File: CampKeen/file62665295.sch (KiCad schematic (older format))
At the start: 23 parts

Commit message: updated the pin mapping to the terms. cleaned up the Schematic. PCB placement and routing is what is left to do.
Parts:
- C16, C17, C18, C19: renamed from C?; footprint (none) -> Capacitor_THT:C_Disc_D4.7mm_W2.5mm_P5.00mm
- Q4: renamed from Q?; footprint TO254P469X1042X1967-3P -> SamacSys_Parts:TO254P469X1042X1967-3P
- Z1: renamed from Z?; footprint DIOAD1068W53L380D172 -> SamacSys_Parts:DIOAD1068W53L380D172
- gave numbers to parts that had none: 17

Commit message: separated the 12 and 5 volt outputs. added another spare output.
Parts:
- renumbered Q3 to Q2, Q4 to Q3, Q5 to Q4, Q6 to Q5, Q7 to Q6, Q8 to Q7, R12 to R15, R13 to R16, R14 to R17, R15 to R18, R16 to R19, R17 to R20, R18 to R21, R19 to R22, R20 to R23, R21 to R24, R22 to R25

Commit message: some annotation.
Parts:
- removed Tanks1: TanksVS, SamacSys_Parts:BK_HTC-15M, symbol SamacSys_Parts:BK_HTC-15M
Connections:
- net +BATT: now also Q3.3, R16.1, Z1.1
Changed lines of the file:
@@
 $Descr A4 11693 8268
 encoding utf-8
-Sheet 2 10
+Sheet 5 10
 Title ""
 Date ""
@@
 Connection ~ 6350 3200
 $Comp
-L SamacSys_Parts:BK_HTC-15M Tanks1
-U 1 1 626F6AAA
-P 4200 1800
-AR Path="/62665296/626F6AAA" Ref="Tanks1"  Part="1"
-AR Path="/6479D118/626F6AAA" Ref="Tanks2"  Part="1"
-F 0 "Tanks2" H 4828 1796 50  0000 L CNN
-F 1 "TanksVS" H 4828 1705 50  0000 L CNN
-F 2 "SamacSys_Parts:BK_HTC-15M" H 4850 1900 50  0001 L CNN
-F 3 "" H 4850 1800 50  0001 L CNN
-F 4 "Fuse Holder PCB FUSE BLOCK" H 4850 1700 50  0001 L CNN "Description"
-F 5 "" H 4850 1600 50  0001 L CNN "Height"
-F 6 "504-HTC-15M" H 4850 1500 50  0001 L CNN "Mouser Part Number"
-F 7 "https://www.mouser.co.uk/ProductDetail/Bussmann-Eaton/BK-HTC-15M?qs=xYgILgh9YcIcij8kQUilpQ%3D%3D" H 4850 1400 50  0001 L CNN "Mouser Price/Stock"
-F 8 "Eaton" H 4850 1300 50  0001 L CNN "Manufacturer_Name"
-F 9 "BK/HTC-15M" H 4850 1200 50  0001 L CNN "Manufacturer_Part_Number"
-	1    4200 1800
-	0    -1   -1   0
-$EndComp
-$Comp
 L power:+BATT #PWR065
 U 1 1 626F6AB0
-P 4200 2100
+P 3850 1700
 AR Path="/62665296/626F6AB0" Ref="#PWR065"  Part="1"
 AR Path="/6479D118/626F6AB0" Ref="#PWR088"  Part="1"
-F 0 "#PWR088" H 4200 1950 50  0001 C CNN
-F 1 "+BATT" H 4215 2273 50  0000 C CNN
-F 2 "" H 4200 2100 50  0001 C CNN
-F 3 "" H 4200 2100 50  0001 C CNN
-	1    4200 2100
-	0    -1   -1   0
-$EndComp
-Wire Wire Line
-	4200 2100 4300 2100
-Wire Wire Line
-	4300 2100 4300 1800
+F 0 "#PWR088" H 3850 1550 50  0001 C CNN
+F 1 "+BATT" H 3865 1873 50  0000 C CNN
+F 2 "" H 3850 1700 50  0001 C CNN
+F 3 "" H 3850 1700 50  0001 C CNN
+	1    3850 1700
+	-1   0    0    -1
+$EndComp
+Wire Wire Line
+	3850 1700 3850 1800
 $Comp
 L SamacSys_Parts:IRF9Z34NPBF Q3
@@
 Wire Wire Line
 	3250 1800 2750 1800
-Wire Wire Line
-	4200 1800 3850 1800
 Connection ~ 3850 1800
 Text HLabel 5950 2450 0    50   Input ~ 0

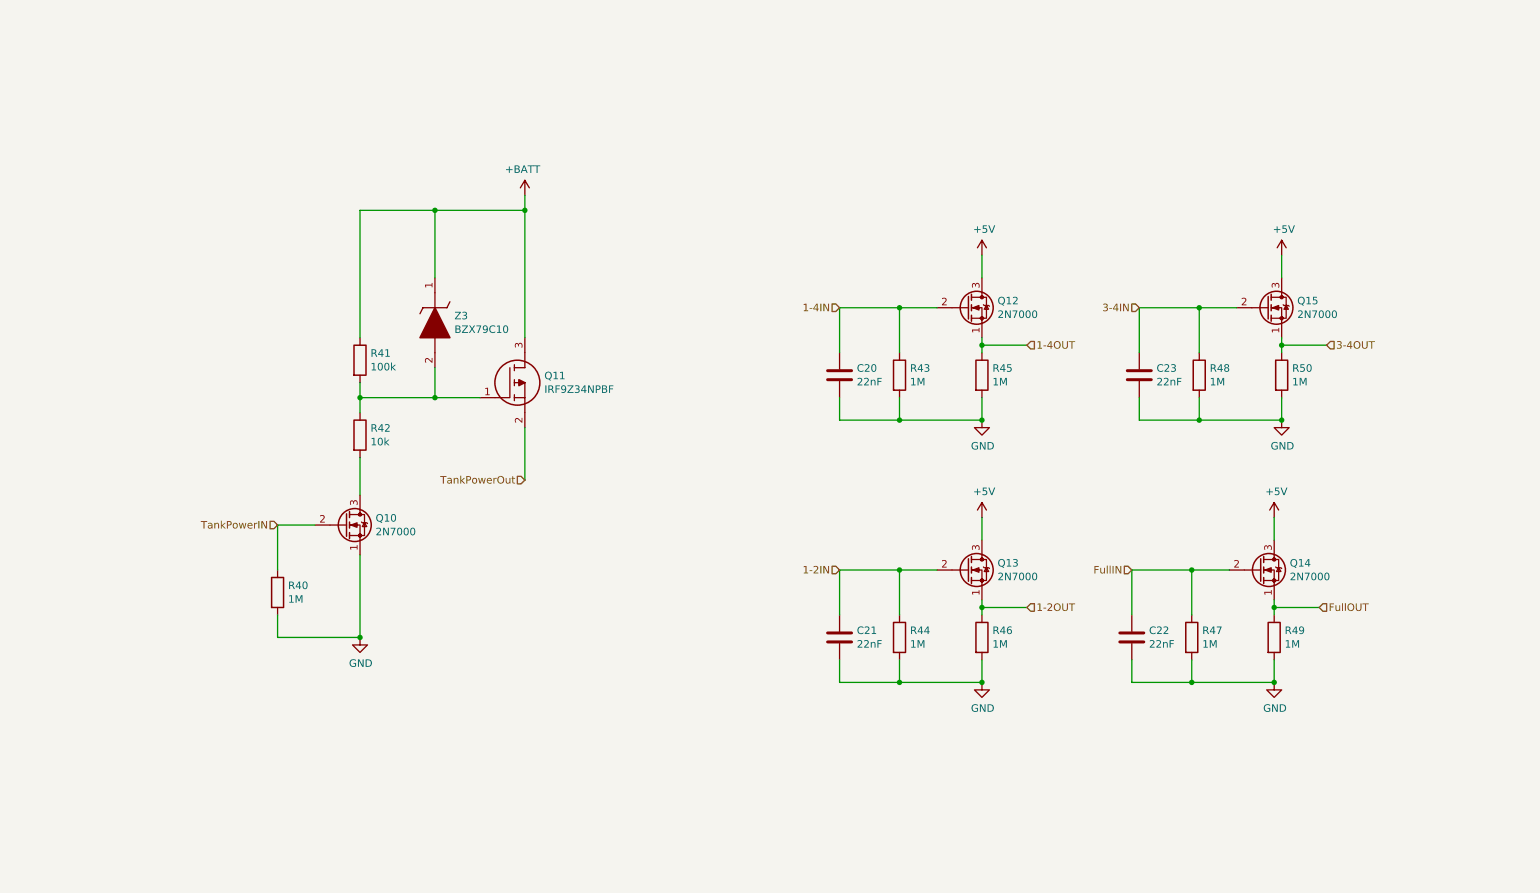
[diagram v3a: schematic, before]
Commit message: schematic done for Input isolation updates.
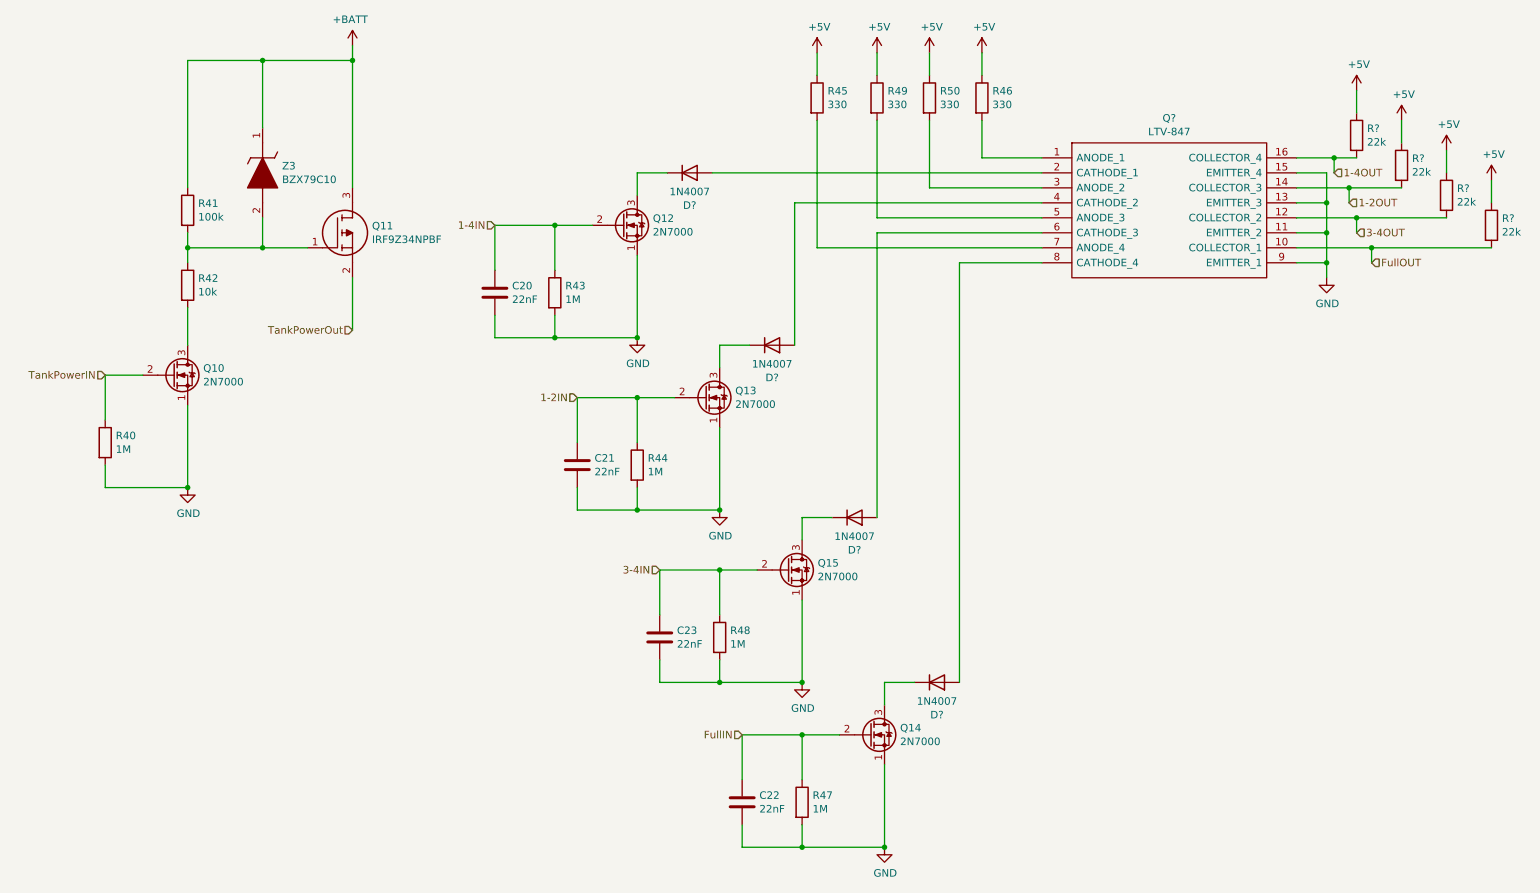
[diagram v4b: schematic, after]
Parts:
- added D? (x4): 1N4007, Diode_THT:D_DO-41_SOD81_P10.16mm_Horizontal, symbol Diode:1N4007
- added Q?: LTV-847, DIP762W60P254L1984H450Q16N, symbol SamacSys_Parts:LTV-847
- added R? (x4): 22k, Resistor_THT:R_Axial_DIN0207_L6.3mm_D2.5mm_P2.54mm_Vertical, symbol Device:R
- R20, R21, R24, R25: value 1M -> 330
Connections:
- net +5V: now also R20.1, R21.1, R24.1, R25.1, R?.1, R?.1, R?.1, R?.1; no longer Q4.3 (D), Q5.3 (D), Q6.3 (D), Q7.3 (D)
- net 1-2OUT: now also Q?.14 (COLLECTOR_3), R?.2; no longer Q5.1 (S), R21.1
- net 1-4OUT: now also Q?.16 (COLLECTOR_4), R?.2; no longer Q4.1 (S), R20.1
- net 3-4OUT: now also Q?.12 (COLLECTOR_2), R?.2; no longer Q7.1 (S), R25.1
- net FullOUT: now also Q?.10 (COLLECTOR_1), R?.2; no longer Q6.1 (S), R24.1
- net GND: now also Q4.1 (S), Q5.1 (S), Q6.1 (S), Q7.1 (S), Q?.11 (EMITTER_2), Q?.13 (EMITTER_3), Q?.15 (EMITTER_4), Q?.9 (EMITTER_1); no longer R20.2, R21.2, R24.2, R25.2
- new net: D?.1 (K), Q4.3 (D)
- new net: D?.2 (A), Q?.2 (CATHODE_1)
- new net: D?.1 (K), Q5.3 (D)
- new net: D?.2 (A), Q?.4 (CATHODE_2)
- new net: D?.1 (K), Q6.3 (D)
- new net: D?.2 (A), Q?.8 (CATHODE_4)
- new net: D?.1 (K), Q7.3 (D)
- new net: D?.2 (A), Q?.6 (CATHODE_3)
- new net: Q?.1 (ANODE_1), R21.2
- new net: Q?.3 (ANODE_2), R25.2
- new net: Q?.5 (ANODE_3), R24.2
- new net: Q?.7 (ANODE_4), R20.2
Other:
- moved on the sheet: C20, C21, C22, C23, Q10, Q11, Q12, Q13, Q14, Q15, R40, R41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

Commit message: added the appropriate power flags to the voltage rails as to make DRC Happy.
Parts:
- gave numbers to parts that had none: 9
